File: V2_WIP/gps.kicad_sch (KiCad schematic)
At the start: 15 parts

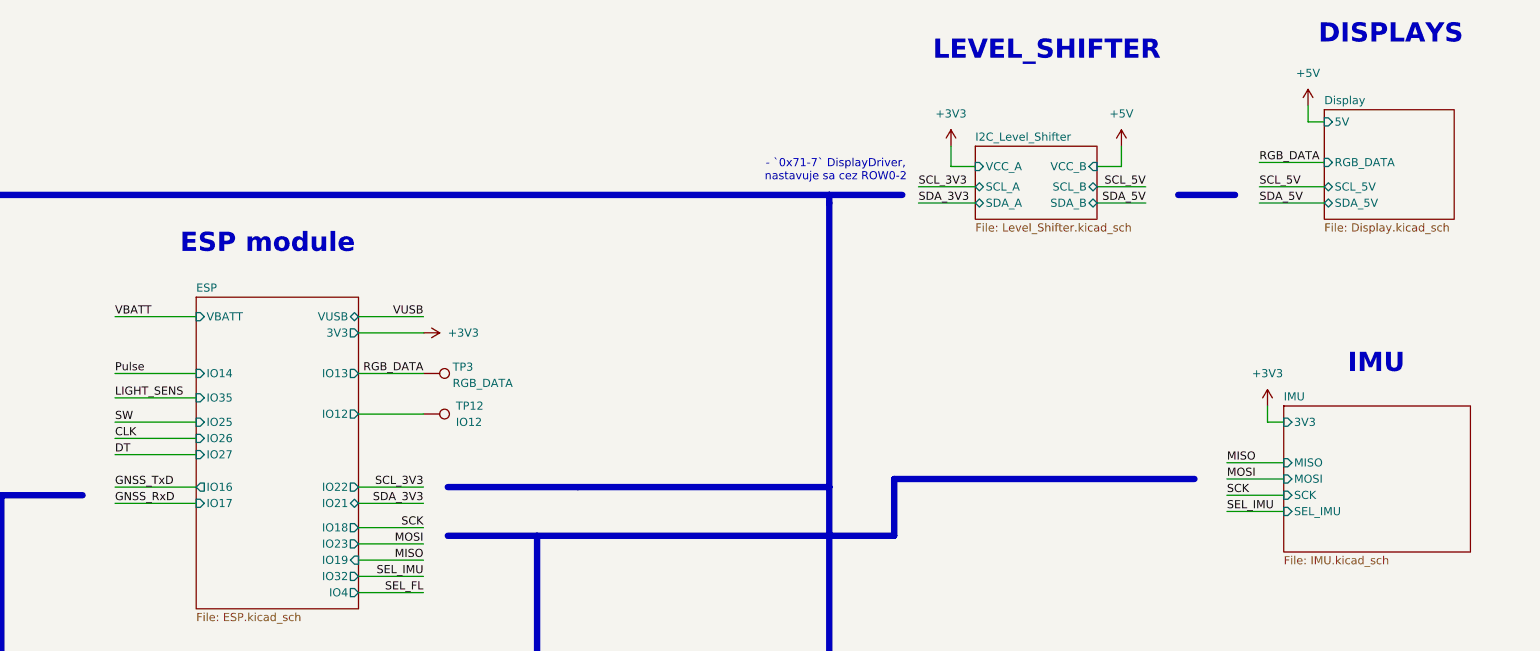
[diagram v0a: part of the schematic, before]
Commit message: added second LDO
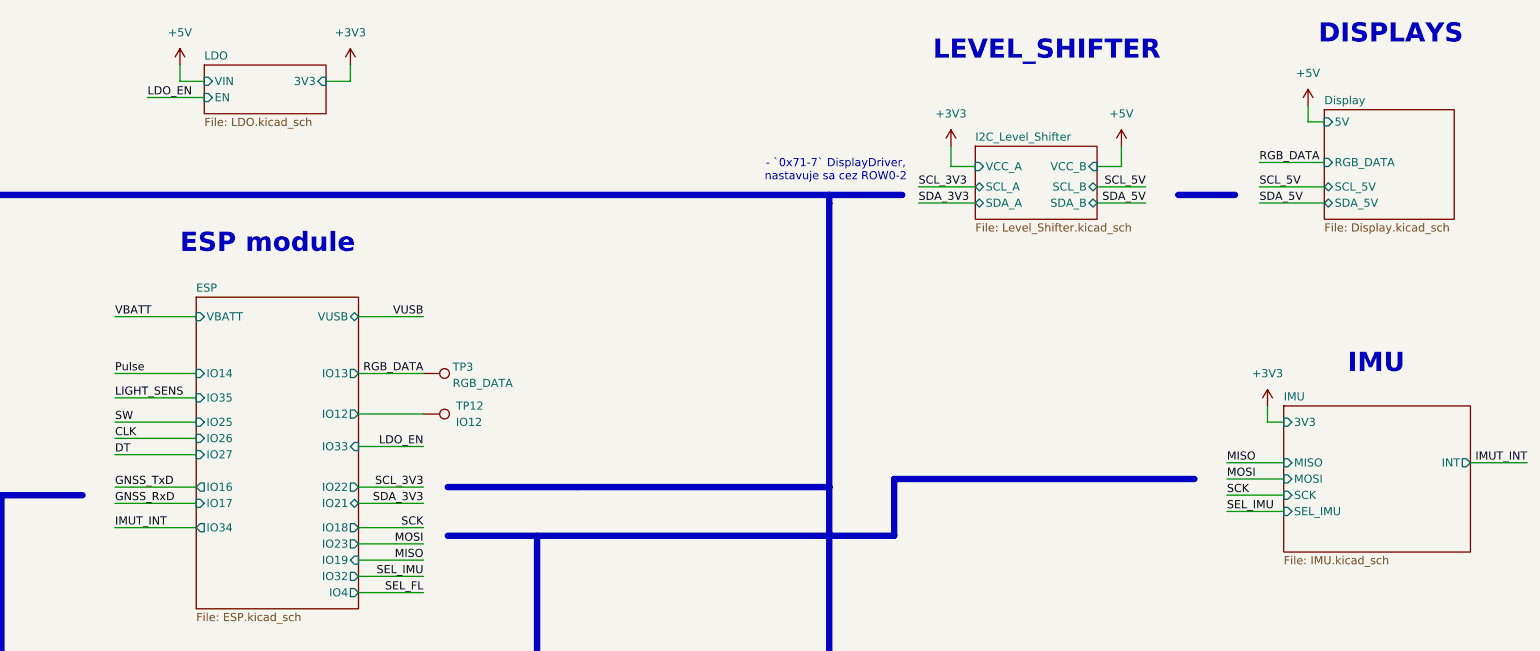
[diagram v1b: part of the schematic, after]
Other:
- added sheet LDO (LDO.kicad_sch)
- sheet ESP ports: added IO33, IO34; removed 3V3
- sheet IMU ports: added INT; removed none

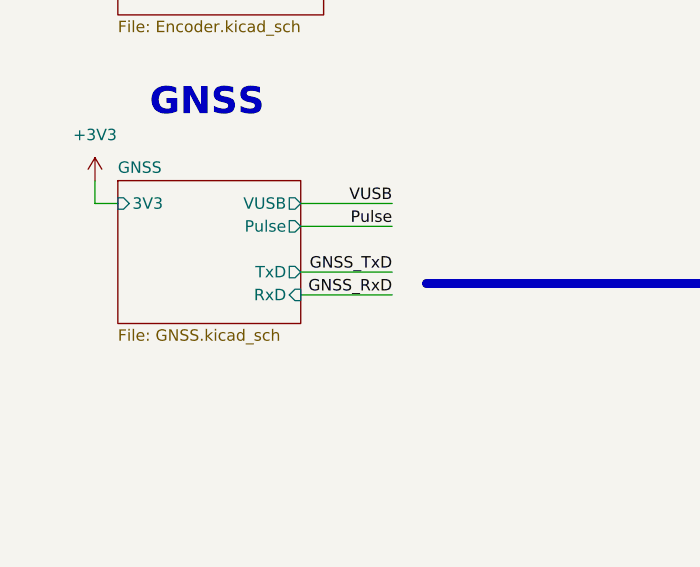
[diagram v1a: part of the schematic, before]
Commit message: switched Tx and Rx on GNSS module, added option to switch them, minor pcb changes
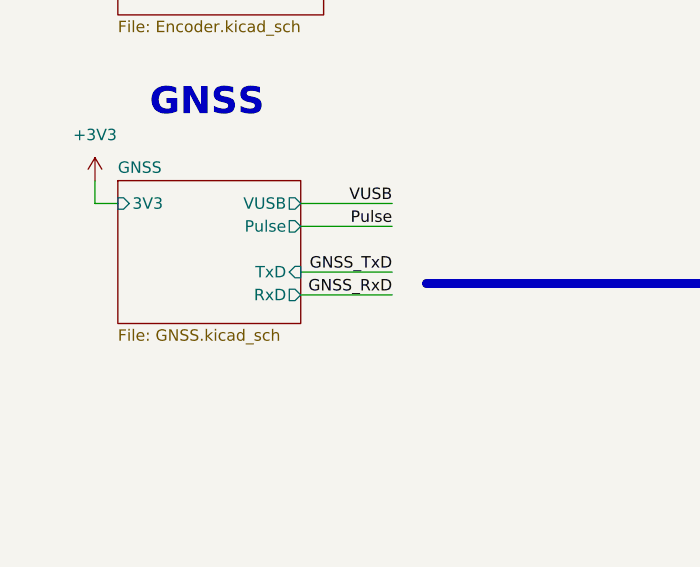
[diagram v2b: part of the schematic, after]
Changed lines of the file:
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@@
 			)
 		)
-		(pin "TxD" output
+		(pin "TxD" input
 			(at 77.47 191.77 0)
 			(effects
@@
 			)
 		)
-		(pin "RxD" input
+		(pin "RxD" output
 			(at 77.47 194.31 0)
 			(effects

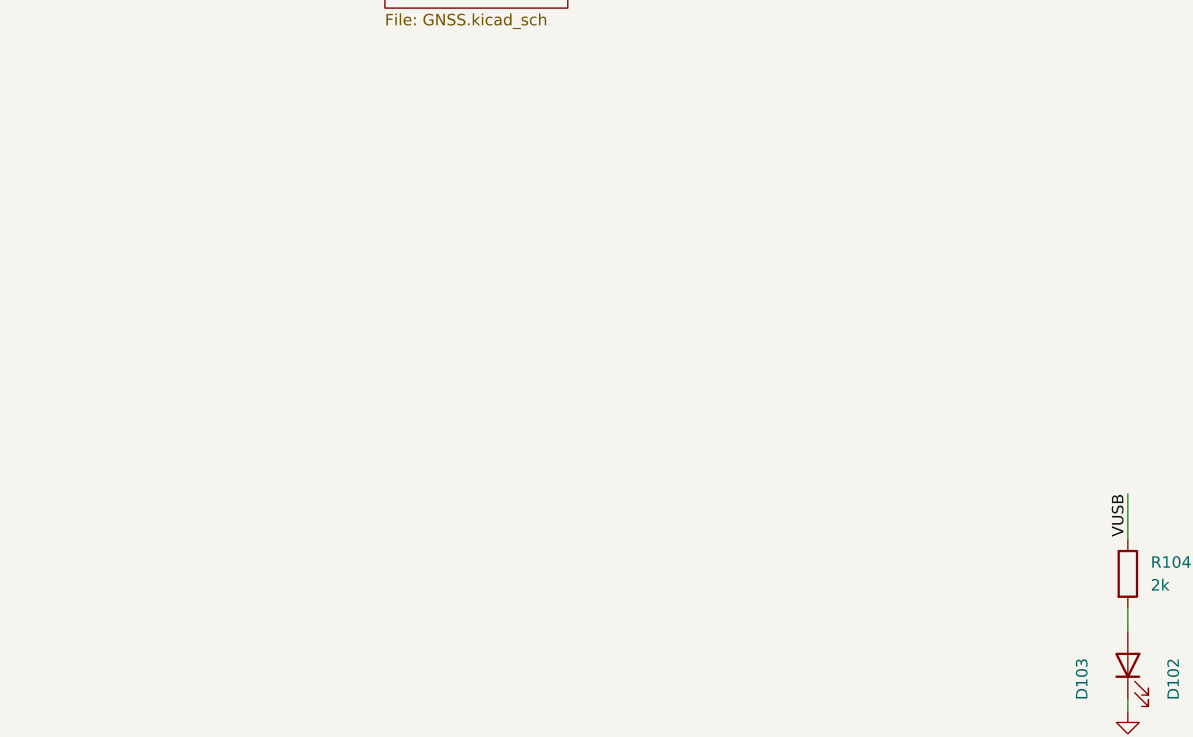
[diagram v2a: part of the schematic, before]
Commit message: added 24 to 5V DCDC
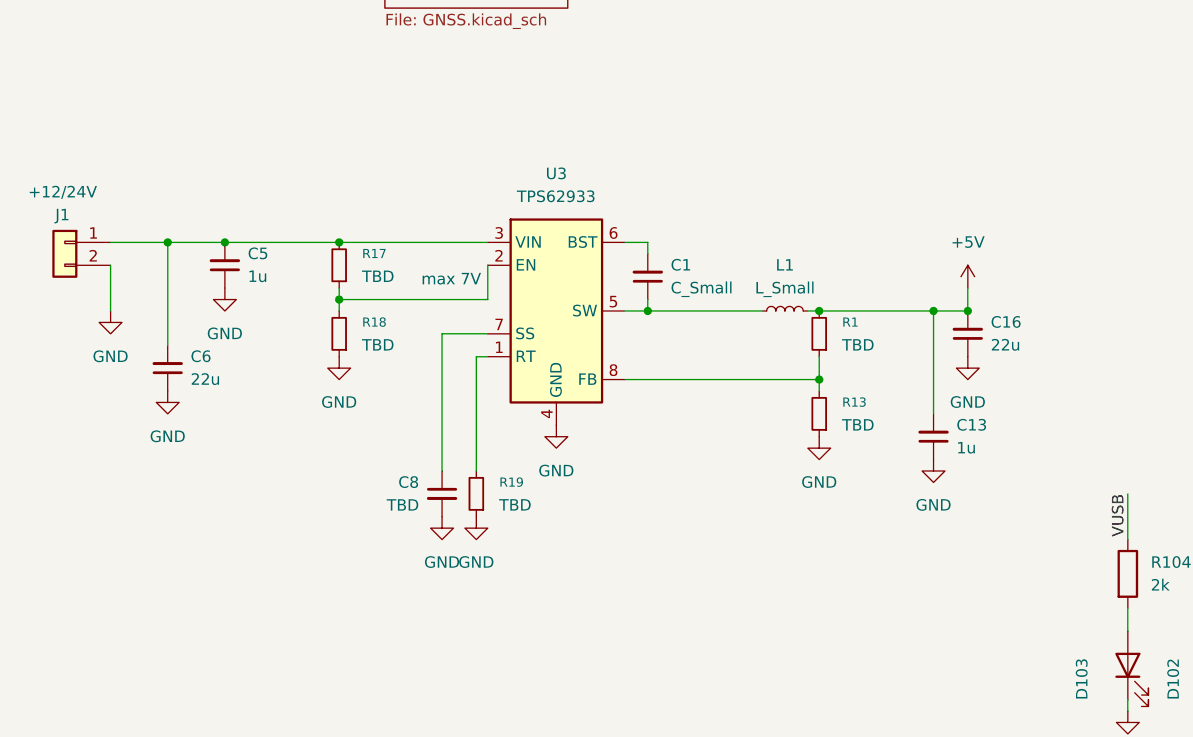
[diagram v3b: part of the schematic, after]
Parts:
- added C1: C_Small, Capacitor_SMD:C_0603_1608Metric_Pad1.08x0.95mm_HandSolder, symbol Device:C_Small
- added C13, C5: 1u, Capacitor_SMD:C_0603_1608Metric_Pad1.08x0.95mm_HandSolder, symbol Device:C_Small
- added C16, C6: 22u, Capacitor_SMD:C_0805_2012Metric_Pad1.18x1.45mm_HandSolder, symbol Device:C_Small
- added C8: TBD, Capacitor_SMD:C_0603_1608Metric_Pad1.08x0.95mm_HandSolder, symbol Device:C_Small
- added J1: +12/24V, Connector_Phoenix_GMSTB:PhoenixContact_GMSTBVA_2,5_2-G-7,62_1x02_P7.62mm_Vertical, symbol Connector_Generic:Conn_01x02
- added L1: L_Small, Inductor_SMD:L_Wuerth_XHMI-6060, symbol Device:L_Small
- added R1, R13, R17, R18, R19: TBD, Resistor_SMD:R_0603_1608Metric_Pad0.98x0.95mm_HandSolder, symbol Device:R_Small
- added U3: TPS62933, Package_TO_SOT_SMD:SOT-583-8, symbol Regulator_Switching:TPS62933
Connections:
- net +5V: now also C13.2, C16.2, L1.2, R1.2
- net GND: now also C13.1, C16.1, C5.1, C6.1, C8.2, J1.2 (Pin_2), R13.1, R18.1, R19.1, U3.4 (GND)
- new net: C8.1, U3.7 (SS)
- new net: R1.1, R13.2, U3.8 (FB)
- new net: C5.2, C6.2, J1.1 (Pin_1), R17.2, U3.3 (VIN)
- new net: C1.1, L1.1, U3.5 (SW)
- new net: C1.2, U3.6 (BST)
- new net: R19.2, U3.1 (RT)
- new net: R17.1, R18.2, U3.2 (EN)
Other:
- note added: "max 7V"

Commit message: added magnetometer
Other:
- added sheet MAGNETOMETER (MAGNETOMETER.kicad_sch)
- note added: "- `0x30` Magnetometer"
- note added: "MAGNETOMETER"

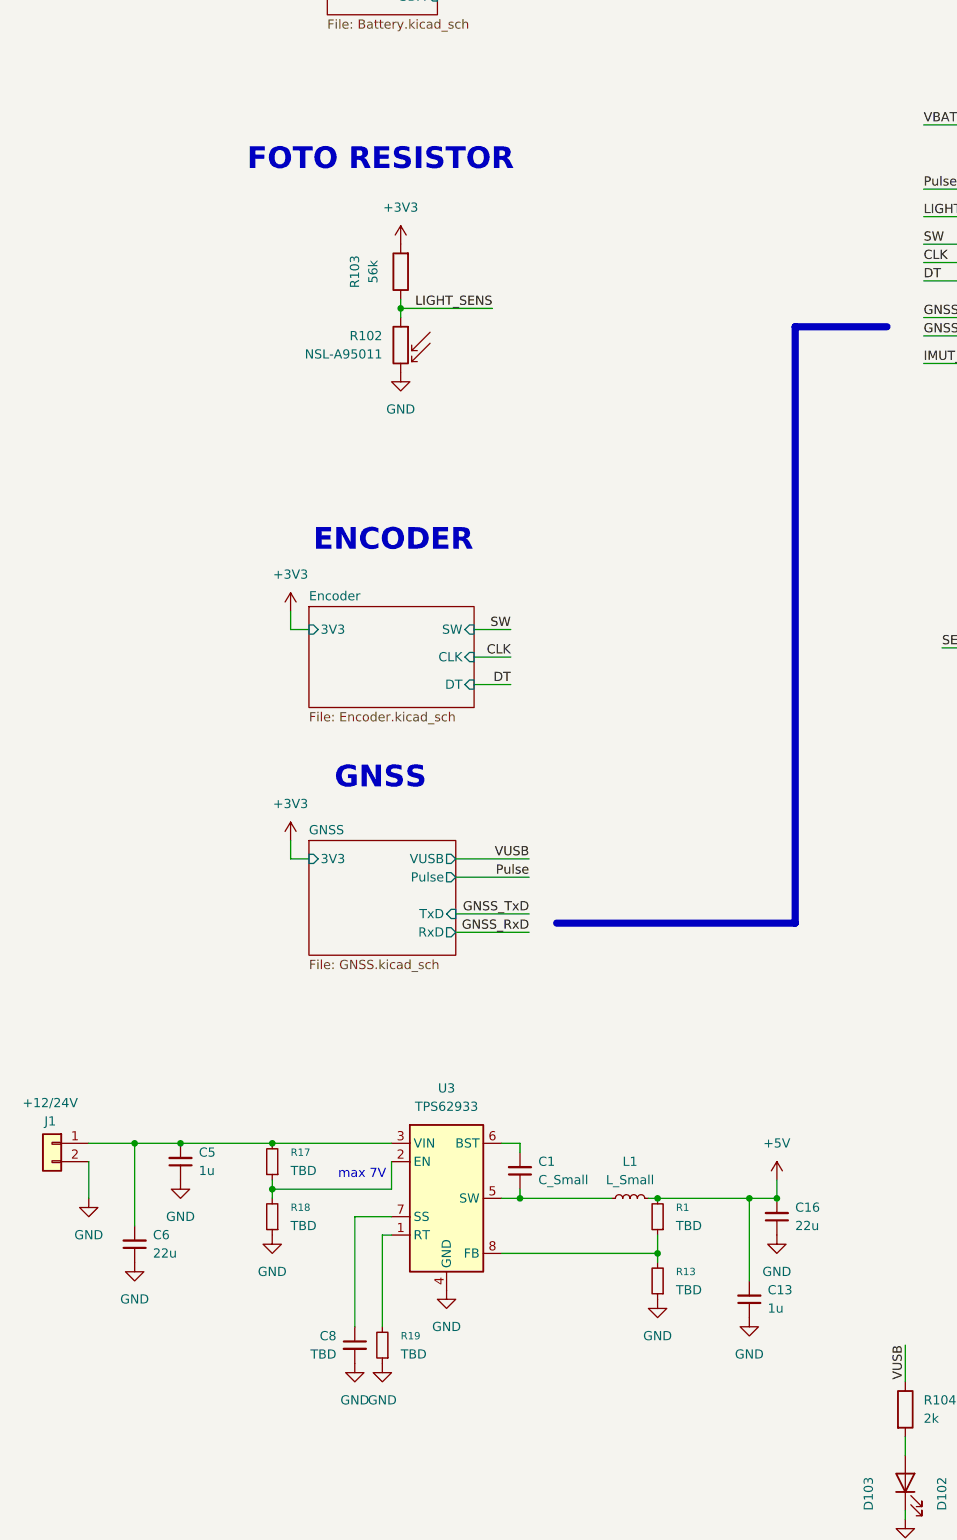
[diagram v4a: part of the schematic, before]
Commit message: moved DCDC to its sheet, added elec capacitor to DCDC
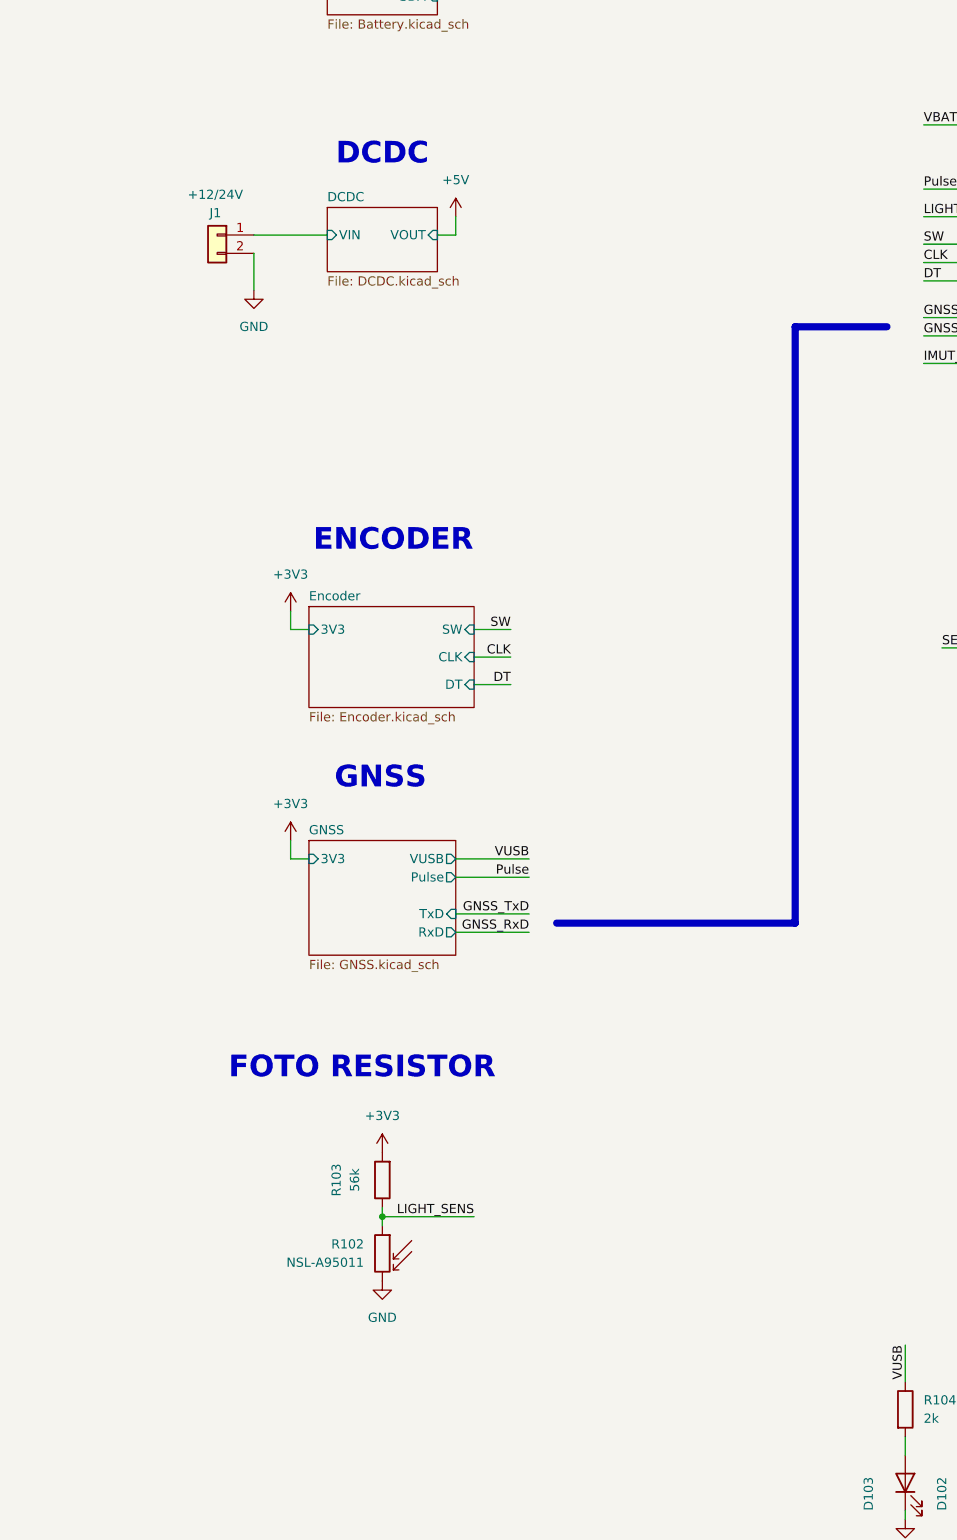
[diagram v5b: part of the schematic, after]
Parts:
- removed C1: C_Small, Capacitor_SMD:C_0603_1608Metric_Pad1.08x0.95mm_HandSolder, symbol Device:C_Small
- removed C13, C5: 1u, Capacitor_SMD:C_0603_1608Metric_Pad1.08x0.95mm_HandSolder, symbol Device:C_Small
- removed C16, C6: 22u, Capacitor_SMD:C_0805_2012Metric_Pad1.18x1.45mm_HandSolder, symbol Device:C_Small
- removed C8: TBD, Capacitor_SMD:C_0603_1608Metric_Pad1.08x0.95mm_HandSolder, symbol Device:C_Small
- removed L1: L_Small, Inductor_SMD:L_Wuerth_XHMI-6060, symbol Device:L_Small
- removed R1, R13, R17, R18, R19: TBD, Resistor_SMD:R_0603_1608Metric_Pad0.98x0.95mm_HandSolder, symbol Device:R_Small
- removed U3: TPS62933, Package_TO_SOT_SMD:SOT-583-8, symbol Regulator_Switching:TPS62933
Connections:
- net DCDC/VIN: now reaches J1.1 (Pin_1)
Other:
- added sheet DCDC (DCDC.kicad_sch)
- note added: "DCDC"
- note removed: "max 7V"
- moved on the sheet: R102, R103
